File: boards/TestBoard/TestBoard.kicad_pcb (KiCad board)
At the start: 2 copper layers, 27 x 69 mm, 26 parts, among them J1 Conn_01x04, J10 Conn_01x02, J11 Conn_01x02, J2 Conn_01x04, J3 Conn_01x80, J4 Conn_01x02, J5 Conn_01x80, U1 MCP23017_ML, U2 MCP23017_ML, U3 MCP23017_ML, U4 MCP23017_ML, U5 MCP23017_ML

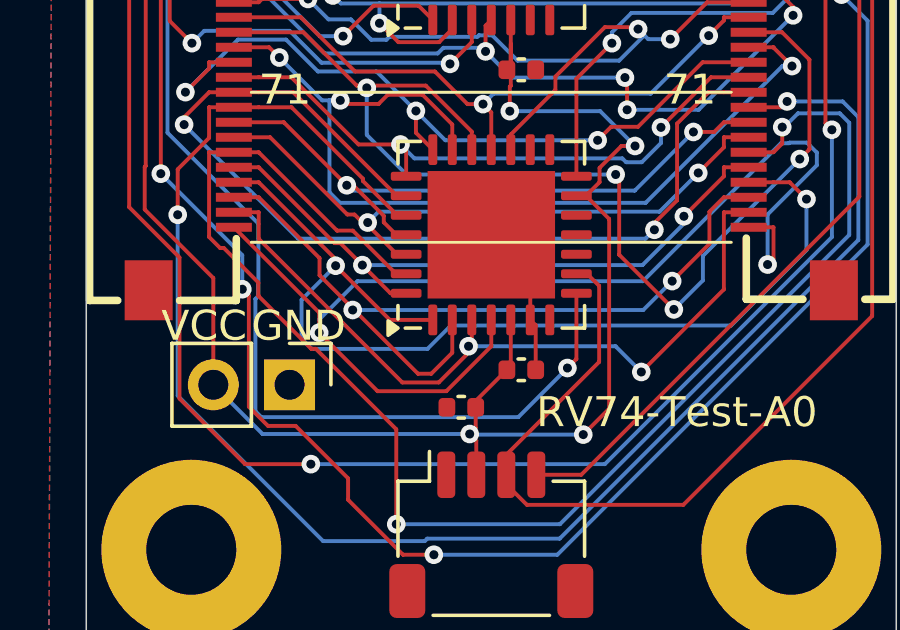
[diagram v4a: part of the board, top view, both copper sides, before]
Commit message: Yet another attempt to resolve this particular silk screen / pad clearance violation
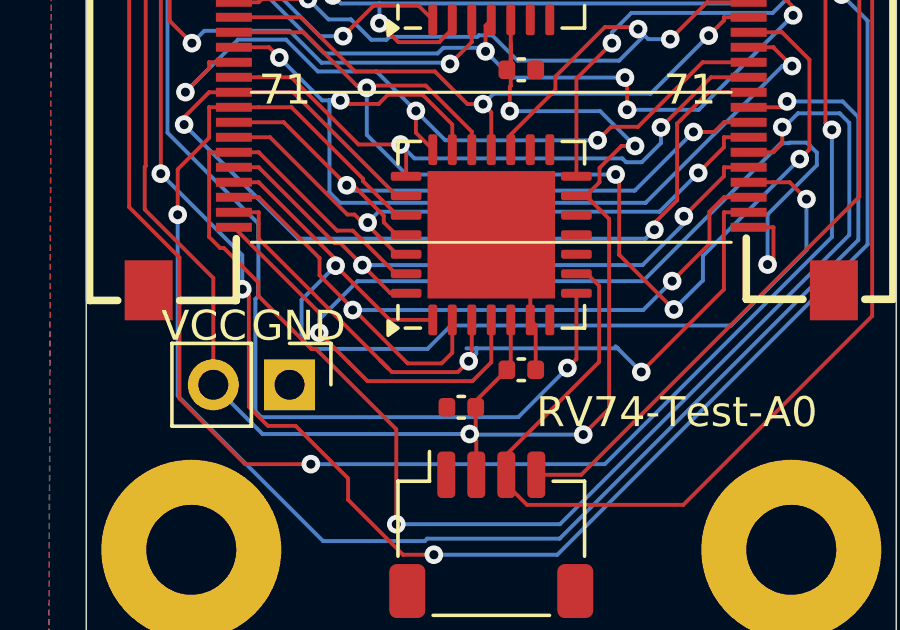
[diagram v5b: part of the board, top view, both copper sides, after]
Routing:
- net /A78: track 25.6 -> 26.6 mm
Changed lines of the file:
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@@
 	)
 	(segment
-		(start 136.5356 88.423)
-		(end 137.75 88.423)
+		(start 138.746697 87.715)
+		(end 138.383697 88.078)
+		(width 0.13)
+		(layer "F.Cu")
+		(net 23)
+	)
+	(segment
+		(start 135.8063 87.6937)
+		(end 136.0563 87.9437)
 		(width 0.13)
 		(layer "F.Cu")
@@
 	)
 	(segment
-		(start 137.75 88.423)
-		(end 138.85 87.323)
+		(start 138.85 87.611697)
+		(end 138.746697 87.715)
 		(width 0.13)
 		(layer "F.Cu")
@@
 	)
 	(segment
-		(start 138.85 87.323)
-		(end 138.85 86.3375)
+		(start 138.85 86.3375)
+		(end 138.85 87.611697)
+		(width 0.13)
+		(layer "F.Cu")
+		(net 23)
+	)
+	(segment
+		(start 136.1906 88.078)
+		(end 135.8063 87.6937)
 		(width 0.13)
 		(layer "F.Cu")
@@
 	(segment
 		(start 131.7467 83.6341)
-		(end 136.5356 88.423)
+		(end 135.8063 87.6937)
+		(width 0.13)
+		(layer "F.Cu")
+		(net 23)
+	)
+	(segment
+		(start 138.383697 88.078)
+		(end 136.1906 88.078)
 		(width 0.13)
 		(layer "F.Cu")
@@
 	)
 	(via
-		(at 138.742197 87.215197)
+		(at 138.746697 87.715)
 		(size 0.62)
 		(drill 0.3)
@@
 	(segment
 		(start 144.501 88.0735)
+		(end 143.71375 87.28625)
+		(width 0.13)
+		(layer "B.Cu")
+		(net 23)
+	)
+	(segment
+		(start 139 87.28625)
+		(end 138.671147 87.28625)
+		(width 0.13)
+		(layer "B.Cu")
+		(net 23)
+	)
+	(segment
+		(start 139 87.461697)
+		(end 138.746697 87.715)
+		(width 0.13)
+		(layer "B.Cu")
+		(net 23)
+	)
+	(segment
+		(start 139 87.28625)
+		(end 139 87.461697)
+		(width 0.13)
+		(layer "B.Cu")
+		(net 23)
+	)
+	(segment
+		(start 143.71375 87.28625)
 		(end 143.642697 87.215197)
 		(width 0.13)
@@
 	)
 	(segment
-		(start 143.642697 87.215197)
-		(end 138.742197 87.215197)
+		(start 143.71375 87.28625)
+		(end 139 87.28625)
 		(width 0.13)
 		(layer "B.Cu")
@@
 	)
 	(segment
-		(start 138 88.714)
-		(end 139.5 87.214)
-		(width 0.13)
-		(layer "F.Cu")
-		(net 25)
-	)
-	(segment
 		(start 133.7634 86.0934)
 		(end 133.7634 86.7687)
@@
 	(segment
 		(start 133.7634 86.7687)
-		(end 135.7087 88.714)
+		(end 134.74735 87.75265)
+		(width 0.13)
+		(layer "F.Cu")
+		(net 25)
+	)
+	(segment
+		(start 138.87235 88.37765)
+		(end 135.37235 88.37765)
 		(width 0.13)
 		(layer "F.Cu")
@@
 	)
 	(segment
-		(start 135.7087 88.714)
-		(end 138 88.714)
+		(start 135.37235 88.37765)
+		(end 134.74735 87.75265)
+		(width 0.13)
+		(layer "F.Cu")
+		(net 25)
+	)
+	(segment
+		(start 139.5 87.75)
+		(end 138.87235 88.37765)
 		(width 0.13)
 		(layer "F.Cu")
@@
 	)
 	(segment
+		(start 139.5 86.3375)
+		(end 139.5 87.75)
+		(width 0.13)
+		(layer "F.Cu")
+		(net 25)
+	)
+	(segment
 		(start 130.92 83.25)
 		(end 133.7634 86.0934)
-		(width 0.13)
-		(layer "F.Cu")
-		(net 25)
-	)
-	(segment
-		(start 139.5 87.214)
-		(end 139.5 86.3375)
 		(width 0.13)
 		(layer "F.Cu")
@@
 	)
 	(segment
+		(start 137.845 87.787)
+		(end 138.2 87.432)
+		(width 0.13)
+		(layer "F.Cu")
+		(net 26)
+	)
+	(segment
 		(start 131.7467 82.25)
 		(end 133.7754 84.2787)
@@
 	)
 	(segment
-		(start 137.5 88.132)
-		(end 138.2 87.432)
-		(width 0.13)
-		(layer "F.Cu")
-		(net 26)
-	)
-	(segment
 		(start 145.5292 85.0437)
 		(end 146.7717 83.8012)
@@
 	)
 	(segment
-		(start 134.9065 85.9805)
-		(end 137.058 88.132)
+		(start 136.713 87.787)
+		(end 137.845 87.787)
 		(width 0.13)
 		(layer "F.Cu")
@@
 	)
 	(segment
+		(start 134.9065 85.9805)
+		(end 136.713 87.787)
+		(width 0.13)
+		(layer "F.Cu")
+		(net 26)
+	)
+	(segment
 		(start 133.7754 84.8494)
 		(end 134.9065 85.9805)
 		(width 0.13)
 		(layer "F.Cu")
-		(net 26)
-	)
-	(segment
-		(start 137.058 88.132)
-		(end 137.5 88.132)
-		(width 0.13)
-		(layer "F.Cu")

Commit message: Fixed some track loose ends
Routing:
- net /A78: track 26.6 -> 25.7 mm
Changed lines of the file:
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@@
 	)
 	(segment
-		(start 138.746697 87.715)
-		(end 138.383697 88.078)
-		(width 0.13)
-		(layer "F.Cu")
-		(net 23)
-	)
-	(segment
-		(start 135.8063 87.6937)
-		(end 136.0563 87.9437)
+		(start 131.7467 82.75)
+		(end 130.92 82.75)
 		(width 0.13)
 		(layer "F.Cu")
@@
 	)
 	(segment
-		(start 131.7467 82.75)
-		(end 131.7467 83.6341)
-		(width 0.13)
-		(layer "F.Cu")
-		(net 23)
-	)
-	(segment
-		(start 130.92 82.75)
-		(end 131.7467 82.75)
-		(width 0.13)
-		(layer "F.Cu")
-		(net 23)
-	)
-	(segment
 		(start 138.85 86.3375)
 		(end 138.85 87.611697)
@@
 	)
 	(segment
-		(start 136.1906 88.078)
-		(end 135.8063 87.6937)
+		(start 138.746697 87.715)
+		(end 138.383697 88.078)
+		(width 0.13)
+		(layer "F.Cu")
+		(net 23)
+	)
+	(segment
+		(start 138.383697 88.078)
+		(end 136.1906 88.078)
+		(width 0.13)
+		(layer "F.Cu")
+		(net 23)
+	)
+	(segment
+		(start 131.7467 83.6341)
+		(end 131.7467 82.75)
 		(width 0.13)
 		(layer "F.Cu")
@@
 	)
 	(segment
-		(start 131.7467 83.6341)
-		(end 135.8063 87.6937)
-		(width 0.13)
-		(layer "F.Cu")
-		(net 23)
-	)
-	(segment
-		(start 138.383697 88.078)
-		(end 136.1906 88.078)
+		(start 136.1906 88.078)
+		(end 131.7467 83.6341)
 		(width 0.13)
 		(layer "F.Cu")
@@
 	)
 	(segment
-		(start 139 87.28625)
-		(end 138.671147 87.28625)
+		(start 143.71375 87.28625)
+		(end 139.175447 87.28625)
 		(width 0.13)
 		(layer "B.Cu")
@@
 	)
 	(segment
-		(start 139 87.461697)
+		(start 139.175447 87.28625)
 		(end 138.746697 87.715)
 		(width 0.13)
 		(layer "B.Cu")
-		(net 23)
-	)
-	(segment
-		(start 139 87.28625)
-		(end 139 87.461697)
-		(width 0.13)
-		(layer "B.Cu")
-		(net 23)
-	)
-	(segment
-		(start 143.71375 87.28625)
-		(end 143.642697 87.215197)
-		(width 0.13)
-		(layer "B.Cu")
-		(net 23)
-	)
-	(segment
-		(start 143.71375 87.28625)
-		(end 139 87.28625)
-		(width 0.13)
-		(layer "B.Cu")
